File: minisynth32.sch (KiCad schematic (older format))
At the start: 19 parts, among them J1 F_PANEL, J2 Conn_02x20_Odd_Even, J3 PJ-002A, J4 ROT_HDR, J5 MIDI_IN, J6 R_BREAKOUT, J7 SSD1306 OLED, SW1 B1, SW2 PB400EEQR1BLK, SW3 B2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

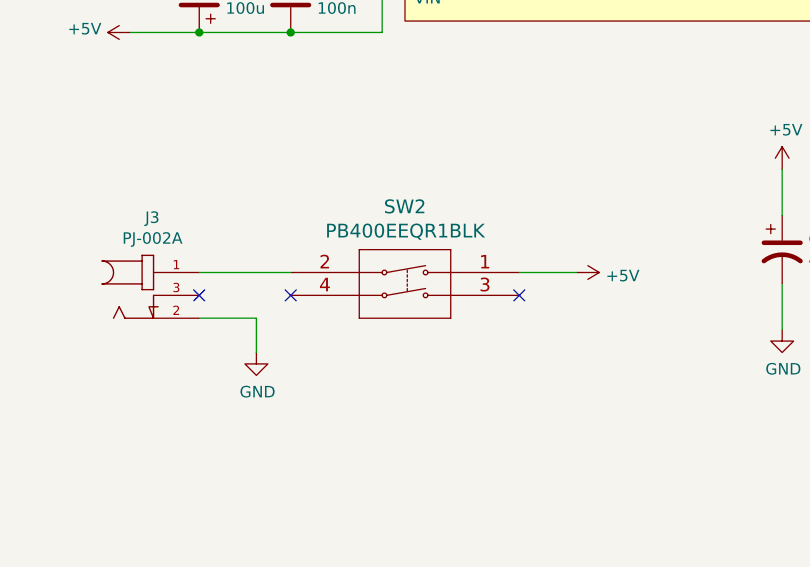
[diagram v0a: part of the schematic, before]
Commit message: PCB rev 1.1 (rear only): cutaway to support RPi3B
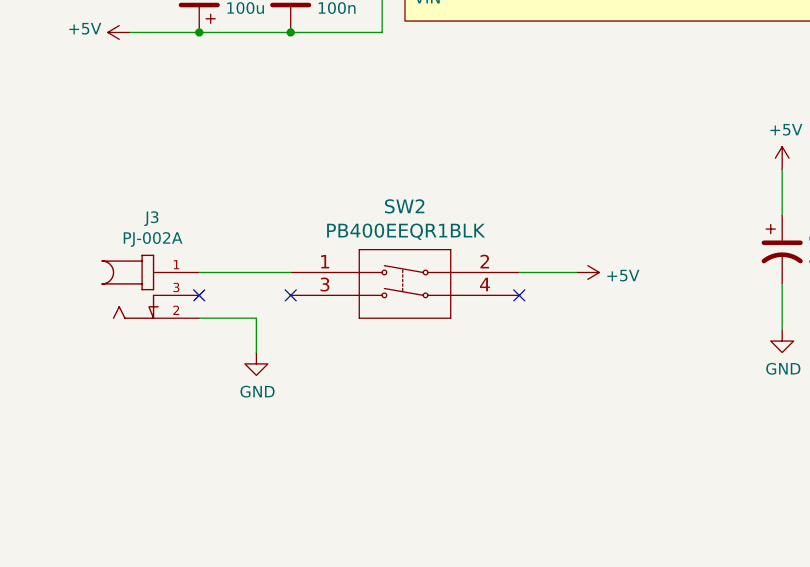
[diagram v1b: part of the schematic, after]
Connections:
- net +5V: now also SW2.2; no longer SW2.1
- net at J3.1: now also SW2.1; no longer SW2.2
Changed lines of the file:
@@
 Title "Minisynth 32: Rear panel breakout and front panel board"
 Date ""
-Rev "1.0"
+Rev "1.1"
 Comp "https://github.com/grantek/minisynth32"
 Comment1 "ClumsyMIDI footprints (c) Andreas Zdziarstek "
@@
 L minisynth32:PB400EEQR1BLK SW2
 U 1 1 60932DE2
-P 9250 5800
-F 0 "SW2" H 9750 6087 60  0000 C CNN
-F 1 "PB400EEQR1BLK" H 9750 5981 60  0000 C CNN
-F 2 "minisynth32:PB400EEQR1BLK" H 9750 5940 60  0001 C CNN
-F 3 "" H 9250 5800 60  0000 C CNN
-	1    9250 5800
-	-1   0    0    -1
-$EndComp
-$Comp
+P 8250 5800
+F 0 "SW2" H 8750 6087 60  0000 C CNN
+F 1 "PB400EEQR1BLK" H 8750 5981 60  0000 C CNN
+F 2 "minisynth32:PB400EEQR1BLK" H 8750 5940 60  0001 C CNN
+F 3 "" H 8250 5800 60  0000 C CNN
+	1    8250 5800
+	1    0    0    -1
+$EndComp
+$Comp

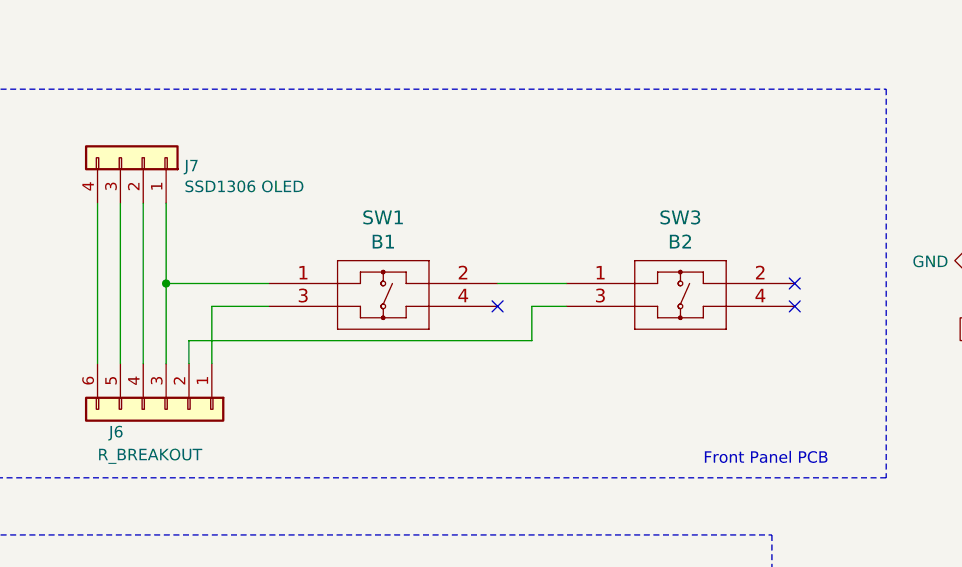
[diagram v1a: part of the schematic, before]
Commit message: Rev 1.1 F/R PCBs, tuned base and top
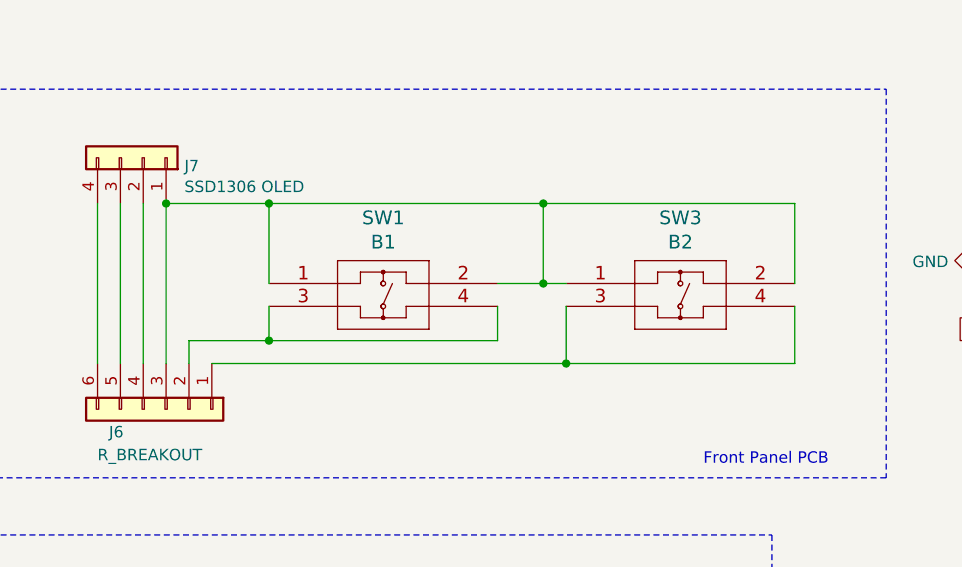
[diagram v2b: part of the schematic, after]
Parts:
- C3: footprint Capacitor_THT:C_Rect_L7.0mm_W2.0mm_P5.00mm -> Capacitor_THT:CP_Radial_D6.3mm_P2.50mm
- R1, R2: footprint Resistor_THT:R_Axial_DIN0207_L6.3mm_D2.5mm_P7.62mm_Horizontal -> Resistor_THT:R_Axial_DIN0207_L6.3mm_D2.5mm_P10.16mm_Horizontal
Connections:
- net at J6.1 (Pin_1): now also SW3.3, SW3.4; no longer SW1.3
- net at J6.2 (Pin_2): now also SW1.3, SW1.4; no longer SW3.3
- net at J6.3 (Pin_3), J7.1 (Pin_1), SW1.1: now also SW1.2, SW3.1, SW3.2
- no-connect marks 33 -> 30
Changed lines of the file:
@@
 F 0 "R2" V 8493 2250 50  0000 C CNN
 F 1 "220R" V 8584 2250 50  0000 C CNN
-F 2 "Resistor_THT:R_Axial_DIN0207_L6.3mm_D2.5mm_P7.62mm_Horizontal" V 8630 2250 50  0001 C CNN
+F 2 "Resistor_THT:R_Axial_DIN0207_L6.3mm_D2.5mm_P10.16mm_Horizontal" V 8630 2250 50  0001 C CNN
 F 3 "~" H 8700 2250 50  0001 C CNN
 	1    8700 2250
@@
 F 0 "R1" V 6807 2700 50  0000 C CNN
 F 1 "1k" V 6716 2700 50  0000 C CNN
-F 2 "Resistor_THT:R_Axial_DIN0207_L6.3mm_D2.5mm_P7.62mm_Horizontal" V 6530 2700 50  0001 C CNN
+F 2 "Resistor_THT:R_Axial_DIN0207_L6.3mm_D2.5mm_P10.16mm_Horizontal" V 6530 2700 50  0001 C CNN
 F 3 "~" H 6600 2700 50  0001 C CNN
 	1    6600 2700
@@
 F 0 "C3" H 7735 4554 50  0000 R CNN
 F 1 "100u" H 7735 4645 50  0000 R CNN
-F 2 "Capacitor_THT:C_Rect_L7.0mm_W2.0mm_P5.00mm" H 7850 4600 50  0001 C CNN
+F 2 "Capacitor_THT:CP_Radial_D6.3mm_P2.50mm" H 7850 4600 50  0001 C CNN
 F 3 "~" H 7850 4600 50  0001 C CNN
 	1    7850 4600
@@
 	1    0    0    -1
 $EndComp
-$Comp
-L minisynth32:TL3301AF160QG SW3
-U 1 1 6097E64C
-P 3350 5450
-F 0 "SW3" H 3850 5737 60  0000 C CNN
-F 1 "B2" H 3850 5631 60  0000 C CNN
-F 2 "minisynth32:TL3301AF160QG-nopaste" H 3850 5590 60  0001 C CNN
-F 3 "" H 3350 5450 60  0000 C CNN
-	1    3350 5450
-	1    0    0    -1
-$EndComp
-NoConn ~ 4350 5450
-NoConn ~ 4350 5550
-NoConn ~ 3050 5550
 Wire Notes Line
 	750  4600 4750 4600
@@
 	750  7400 750  6550
 Wire Wire Line
-	1800 5800 1800 5550
-Wire Wire Line
-	1800 5550 2050 5550
-Wire Wire Line
-	1700 5800 1700 5700
-Wire Wire Line
-	1700 5700 3200 5700
-Wire Wire Line
-	3200 5700 3200 5550
-Wire Wire Line
-	3200 5550 3350 5550
-Wire Wire Line
-	1600 5800 1600 5450
-Wire Wire Line
-	1600 5450 2050 5450
-Wire Wire Line
-	1600 5450 1600 5100
-Connection ~ 1600 5450
-Wire Wire Line
 	1500 5800 1500 5100
 Wire Wire Line
@@
 	1300 5800 1300 5100
 Wire Wire Line
-	3050 5450 3350 5450
+	3050 5450 3250 5450
 Text GLabel 5450 5150 0    50   Output ~ 0
 BTN2
@@
 	0    1    1    0
 $EndComp
+Wire Wire Line
+	3250 5100 3250 5450
+Connection ~ 3250 5450
+Wire Wire Line
+	3250 5450 3350 5450
+Wire Wire Line
+	3250 5100 4350 5100
+Wire Wire Line
+	4350 5100 4350 5450
+Connection ~ 3250 5100
+Wire Wire Line
+	1600 5100 2050 5100
+Connection ~ 1600 5100
+Wire Wire Line
+	1600 5100 1600 5800
+Wire Wire Line
+	2050 5450 2050 5100
+Connection ~ 2050 5100
+Wire Wire Line
+	2050 5100 3250 5100
+$Comp
+L minisynth32:TL3301AF160QG SW3
+U 1 1 6097E64C
+P 3350 5450
+F 0 "SW3" H 3850 5737 60  0000 C CNN
+F 1 "B2" H 3850 5631 60  0000 C CNN
+F 2 "minisynth32:TL3301AF160QG-nopaste" H 3850 5590 60  0001 C CNN
+F 3 "" H 3350 5450 60  0000 C CNN
+	1    3350 5450
+	1    0    0    -1
+$EndComp
+Wire Wire Line
+	1800 5800 3350 5800
+Wire Wire Line
+	3350 5800 3350 5550
+Wire Wire Line
+	3350 5800 4350 5800
+Wire Wire Line
+	4350 5800 4350 5550
+Connection ~ 3350 5800
+Wire Wire Line
+	1700 5800 1700 5700
+Wire Wire Line
+	1700 5700 2050 5700
+Wire Wire Line
+	3050 5700 3050 5550
+Wire Wire Line
+	2050 5700 2050 5550
+Connection ~ 2050 5700
+Wire Wire Line
+	2050 5700 3050 5700
 $EndSCHEMATC

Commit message: front pcb v2
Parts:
- removed SW1: B1, minisynth32:TL3301AF160QG-nopaste, symbol minisynth32:TL3301AF160QG
- removed SW3: B2, minisynth32:TL3301AF160QG-nopaste, symbol minisynth32:TL3301AF160QG
- added J8: UNUSED_2, minisynth32:PinHeader_1x04_P2.54mm_Vertical, symbol minisynth32:Connector_Generic_Conn_01x04
- added J9: UNUSED_1, minisynth32:PinHeader_1x04_P2.54mm_Vertical, symbol minisynth32:Connector_Generic_Conn_01x04
- added SW1: B1, minisynth32:TL59N, symbol Switch:SW_Push
- added SW10, SW3, SW4, SW5, SW6, SW7, SW8, SW9: SW_Push, minisynth32:TL59N, symbol Switch:SW_Push
- added SW2: B2, minisynth32:TL59N, symbol Switch:SW_Push
- renumbered SW2 to SW11
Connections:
- net at J6.1 (Pin_1): now also SW1.1
- net at J6.2 (Pin_2): now also SW2.1
- net GND2: now reaches J6.3 (Pin_3), J7.1 (Pin_1)
- net GND2: now also SW1.2, SW10.2, SW2.2, SW3.2, SW4.2, SW5.2, SW6.2, SW7.2, SW8.2, SW9.2
- new net: J9.4 (Pin_4), SW3.1
- new net: J8.4 (Pin_4), SW4.1
- new net: J9.1 (Pin_1), SW5.1
- new net: J9.2 (Pin_2), SW6.1
- new net: J9.3 (Pin_3), SW7.1
- new net: J8.1 (Pin_1), SW8.1
- new net: J8.2 (Pin_2), SW9.1
- new net: J8.3 (Pin_3), SW10.1
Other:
- note added: "UNUSED Front Panel buttons\n\nThese may connect to a future\nversion of mt32-pi, or tactile\nswitches may be placed that\nhave no connection"
- moved on the sheet: J1
